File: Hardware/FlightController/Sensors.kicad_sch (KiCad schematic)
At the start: 7 parts, among them U2 MPU-6050, U5 MMC5603NJ

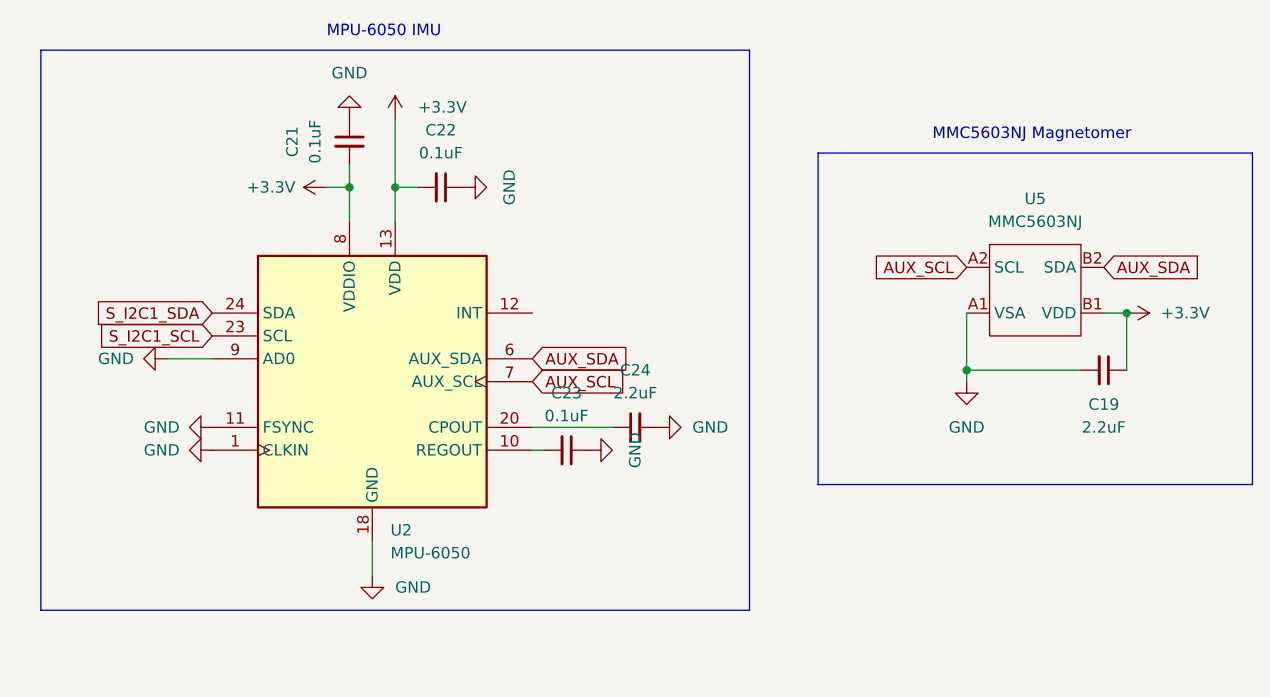
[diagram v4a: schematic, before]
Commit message: Update footprints to be digikey compliant
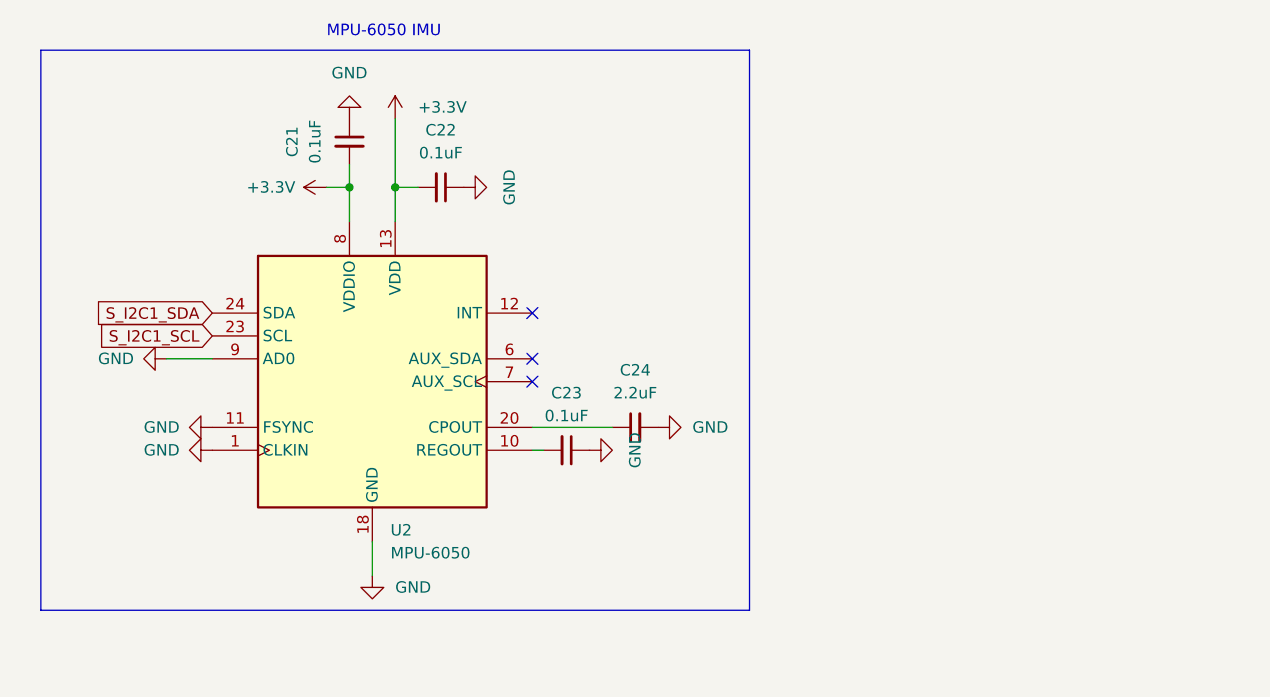
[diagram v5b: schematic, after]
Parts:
- removed C19: 2.2uF, Capacitor_SMD:C_0402_1005Metric, symbol Device:C_Small
- removed U5: MMC5603NJ, Package_BGA:WLP-4_0.83x0.83mm_P0.4mm, symbol FlightControllerLibrary:MMC5603NJ
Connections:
- net AUX_SCL: no longer names the net of U2.7 (AUX_SCL)
- net AUX_SDA: no longer names the net of U2.6 (AUX_SDA)
- no-connect marks 0 -> 3
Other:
- note removed: "MMC5603NJ Magnetomer"
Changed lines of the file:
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@@
   (junction (at 58.42 33.02) (diameter 0) (color 0 0 0 0)
   )
-  (junction (at 121.92 53.34) (diameter 0) (color 0 0 0 0)
-  )
   (junction (at 53.34 33.02) (diameter 0) (color 0 0 0 0)
   )
-  (junction (at 139.7 46.99) (diameter 0) (color 0 0 0 0)
-  )
+  (no_connect (at 73.66 54.61))
+  (no_connect (at 73.66 52.07))
+  (no_connect (at 73.66 46.99))
   (polyline (pts (xy 19.05 80.01) (xy 19.05 17.78))
     (stroke (width 0) (type default) (color 0 0 0 0))
@@
     (stroke (width 0) (type default) (color 0 0 0 0))
   )
-  (wire (pts (xy 121.92 53.34) (xy 134.62 53.34))
-    (stroke (width 0) (type default) (color 0 0 0 0))
-  )
-  (polyline (pts (xy 153.67 66.04) (xy 105.41 66.04))
-    (stroke (width 0) (type default) (color 0 0 0 0))
-  )
-  (polyline (pts (xy 105.41 66.04) (xy 105.41 29.21))
-    (stroke (width 0) (type default) (color 0 0 0 0))
-  )
   (wire (pts (xy 53.34 33.02) (xy 53.34 36.83))
     (stroke (width 0) (type default) (color 0 0 0 0))
   )
-  (wire (pts (xy 137.16 46.99) (xy 139.7 46.99))
-    (stroke (width 0) (type default) (color 0 0 0 0))
-  )
   (wire (pts (xy 55.88 76.2) (xy 55.88 72.39))
     (stroke (width 0) (type default) (color 0 0 0 0))
@@
     (stroke (width 0) (type default) (color 0 0 0 0))
   )
-  (wire (pts (xy 121.92 53.34) (xy 121.92 54.61))
-    (stroke (width 0) (type default) (color 0 0 0 0))
-  )
   (polyline (pts (xy 97.79 80.01) (xy 19.05 80.01))
     (stroke (width 0) (type default) (color 0 0 0 0))
   )
-  (polyline (pts (xy 153.67 29.21) (xy 153.67 66.04))
-    (stroke (width 0) (type default) (color 0 0 0 0))
-  )
-  (wire (pts (xy 139.7 46.99) (xy 139.7 53.34))
-    (stroke (width 0) (type default) (color 0 0 0 0))
-  )
   (wire (pts (xy 58.42 33.02) (xy 58.42 36.83))
     (stroke (width 0) (type default) (color 0 0 0 0))
   )
-  (wire (pts (xy 121.92 46.99) (xy 121.92 53.34))
-    (stroke (width 0) (type default) (color 0 0 0 0))
-  )
   (polyline (pts (xy 97.79 17.78) (xy 97.79 80.01))
     (stroke (width 0) (type default) (color 0 0 0 0))
@@
     (stroke (width 0) (type default) (color 0 0 0 0))
   )
-  (polyline (pts (xy 105.41 29.21) (xy 153.67 29.21))
-    (stroke (width 0) (type default) (color 0 0 0 0))
-  )
   (text "MPU-6050 IMU" (at 50.8 16.51 0)
-    (effects (font (size 1.27 1.27)) (justify left bottom))
-  )
-  (text "MMC5603NJ Magnetomer" (at 118.11 27.94 0)
     (effects (font (size 1.27 1.27)) (justify left bottom))
   )
@@
     )
   )
-  (global_label "AUX_SCL" (shape input) (at 73.66 54.61 0) (fields_autoplaced)
-    (effects (font (size 1.27 1.27)) (justify left))
-    (property "Intersheet References" "${INTERSHEET_REFS}" (id 0) (at 84.1769 54.6894 0)
-      (effects (font (size 1.27 1.27)) (justify left) hide)
-    )
-  )
-  (global_label "AUX_SDA" (shape input) (at 137.16 41.91 0) (fields_autoplaced)
-    (effects (font (size 1.27 1.27)) (justify left))
-    (property "Intersheet References" "${INTERSHEET_REFS}" (id 0) (at 147.7374 41.8306 0)
-      (effects (font (size 1.27 1.27)) (justify left) hide)
-    )
-  )
-  (global_label "AUX_SCL" (shape input) (at 121.92 41.91 180) (fields_autoplaced)
-    (effects (font (size 1.27 1.27)) (justify right))
-    (property "Intersheet References" "${INTERSHEET_REFS}" (id 0) (at 111.4031 41.8306 0)
-      (effects (font (size 1.27 1.27)) (justify right) hide)
-    )
-  )
-  (global_label "AUX_SDA" (shape input) (at 73.66 52.07 0) (fields_autoplaced)
-    (effects (font (size 1.27 1.27)) (justify left))
-    (property "Intersheet References" "${INTERSHEET_REFS}" (id 0) (at 84.2374 51.9906 0)
-      (effects (font (size 1.27 1.27)) (justify left) hide)
-    )
-  )
   (symbol (lib_id "power:+3.3V") (at 58.42 25.4 0) (unit 1)
     (in_bom yes) (on_board yes) (fields_autoplaced)
@@
     )
     (property "Datasheet" "" (id 3) (at 58.42 25.4 0)
-      (effects (font (size 1.27 1.27)) hide)
-    )
-    (pin "1")
-  )
-  (symbol (lib_id "power:+3.3V") (at 139.7 46.99 270) (unit 1)
-    (in_bom yes) (on_board yes) (fields_autoplaced)
-    (property "Reference" "#PWR023" (id 0) (at 135.89 46.99 0)
-      (effects (font (size 1.27 1.27)) hide)
-    )
-    (property "Value" "+3.3V" (id 1) (at 143.51 46.9899 90)
-      (effects (font (size 1.27 1.27)) (justify left))
-    )
-    (property "Footprint" "" (id 2) (at 139.7 46.99 0)
-      (effects (font (size 1.27 1.27)) hide)
-    )
-    (property "Datasheet" "" (id 3) (at 139.7 46.99 0)
       (effects (font (size 1.27 1.27)) hide)
     )
@@
     (pin "2")
   )
-  (symbol (lib_id "Device:C_Small") (at 137.16 53.34 270) (unit 1)
-    (in_bom yes) (on_board yes)
-    (property "Reference" "C19" (id 0) (at 137.16 57.15 90))
-    (property "Value" "2.2uF" (id 1) (at 137.16 59.69 90))
-    (property "Footprint" "Capacitor_SMD:C_0402_1005Metric" (id 2) (at 137.16 53.34 0)
-      (effects (font (size 1.27 1.27)) hide)
-    )
-    (property "Datasheet" "~" (id 3) (at 137.16 53.34 0)
-      (effects (font (size 1.27 1.27)) hide)
-    )
-    (pin "1")
-    (pin "2")
-  )
   (symbol (lib_id "Device:C_Small") (at 63.5 33.02 270) (unit 1)
     (in_bom yes) (on_board yes) (fields_autoplaced)
@@
     (pin "2")
   )
-  (symbol (lib_id "FlightControllerLibrary:MMC5603NJ") (at 129.54 44.45 0) (unit 1)
-    (in_bom yes) (on_board yes) (fields_autoplaced)
-    (property "Reference" "U5" (id 0) (at 129.54 34.29 0))
-    (property "Value" "MMC5603NJ" (id 1) (at 129.54 36.83 0))
-    (property "Footprint" "Package_BGA:WLP-4_0.83x0.83mm_P0.4mm" (id 2) (at 129.54 44.45 0)
-      (effects (font (size 1.27 1.27)) hide)
-    )
-    (property "Datasheet" "" (id 3) (at 129.54 44.45 0)
-      (effects (font (size 1.27 1.27)) hide)
-    )
-    (pin "A1")
-    (pin "A2")
-    (pin "B1")
-    (pin "B2")
-  )
   (symbol (lib_id "Device:C_Small") (at 53.34 27.94 0) (unit 1)
     (in_bom yes) (on_board yes) (fields_autoplaced)
@@
       (effects (font (size 1.27 1.27)) hide)
     )
-    (pin "1")
-  )
-  (symbol (lib_id "power:GND") (at 121.92 54.61 0) (unit 1)
-    (in_bom yes) (on_board yes) (fields_autoplaced)
-    (property "Reference" "#PWR022" (id 0) (at 121.92 60.96 0)
-      (effects (font (size 1.27 1.27)) hide)
-    )
-    (property "Value" "GND" (id 1) (at 121.92 59.69 0))
-    (property "Footprint" "" (id 2) (at 121.92 54.61 0)
-      (effects (font (size 1.27 1.27)) hide)
-    )
-    (property "Datasheet" "" (id 3) (at 121.92 54.61 0)
-      (effects (font (size 1.27 1.27)) hide)
-    )

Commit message: Update footprints, routing and LCSC numbers
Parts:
- C11: renamed from C21; footprint Capacitor_SMD:C_0402_1005Metric -> Capacitor_SMD:C_0603_1608Metric_Pad1.08x0.95mm_HandSolder; dk (none) -> y
- C12: renamed from C22; footprint Capacitor_SMD:C_0402_1005Metric -> Capacitor_SMD:C_0603_1608Metric_Pad1.08x0.95mm_HandSolder; dk (none) -> y
- C13: renamed from C23; footprint Capacitor_SMD:C_0402_1005Metric -> Capacitor_SMD:C_0603_1608Metric_Pad1.08x0.95mm_HandSolder; dk (none) -> y
- C14: renamed from C24; LCSC (none) -> C12530
- U4: renamed from U2; LCSC (none) -> C24112
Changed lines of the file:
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@@
   (symbol (lib_id "power:+3.3V") (at 58.42 25.4 0) (unit 1)
     (in_bom yes) (on_board yes) (fields_autoplaced)
-    (property "Reference" "#PWR034" (id 0) (at 58.42 29.21 0)
+    (property "Reference" "#PWR024" (id 0) (at 58.42 29.21 0)
       (effects (font (size 1.27 1.27)) hide)
     )
@@
   (symbol (lib_id "power:GND") (at 33.02 52.07 270) (unit 1)
     (in_bom yes) (on_board yes)
-    (property "Reference" "#PWR028" (id 0) (at 26.67 52.07 0)
+    (property "Reference" "#PWR018" (id 0) (at 26.67 52.07 0)
       (effects (font (size 1.27 1.27)) hide)
     )
@@
   (symbol (lib_id "power:GND") (at 66.04 33.02 90) (unit 1)
     (in_bom yes) (on_board yes) (fields_autoplaced)
-    (property "Reference" "#PWR035" (id 0) (at 72.39 33.02 0)
+    (property "Reference" "#PWR025" (id 0) (at 72.39 33.02 0)
       (effects (font (size 1.27 1.27)) hide)
     )
@@
   (symbol (lib_id "Device:C_Small") (at 85.09 59.69 90) (unit 1)
     (in_bom yes) (on_board yes) (fields_autoplaced)
-    (property "Reference" "C24" (id 0) (at 85.0963 53.34 90))
+    (property "Reference" "C14" (id 0) (at 85.0963 53.34 90))
     (property "Value" "2.2uF" (id 1) (at 85.0963 55.88 90))
     (property "Footprint" "Capacitor_SMD:C_0402_1005Metric" (id 2) (at 85.09 59.69 0)
@@
       (effects (font (size 1.27 1.27)) hide)
     )
+    (property "LCSC" "C12530" (id 4) (at 85.09 59.69 0)
+      (effects (font (size 1.27 1.27)) hide)
+    )
     (pin "1")
     (pin "2")
@@
   (symbol (lib_id "power:+3.3V") (at 50.8 33.02 90) (unit 1)
     (in_bom yes) (on_board yes)
-    (property "Reference" "#PWR031" (id 0) (at 54.61 33.02 0)
+    (property "Reference" "#PWR021" (id 0) (at 54.61 33.02 0)
       (effects (font (size 1.27 1.27)) hide)
     )
@@
   (symbol (lib_id "Sensor_Motion:MPU-6050") (at 55.88 54.61 0) (unit 1)
     (in_bom yes) (on_board yes) (fields_autoplaced)
-    (property "Reference" "U2" (id 0) (at 57.8994 71.12 0)
+    (property "Reference" "U4" (id 0) (at 57.8994 71.12 0)
       (effects (font (size 1.27 1.27)) (justify left))
     )
@@
     )
     (property "Datasheet" "https://store.invensense.com/datasheets/invensense/MPU-6050_DataSheet_V3%204.pdf" (id 3) (at 55.88 58.42 0)
+      (effects (font (size 1.27 1.27)) hide)
+    )
+    (property "LCSC" "C24112" (id 4) (at 55.88 54.61 0)
       (effects (font (size 1.27 1.27)) hide)
     )
@@
   (symbol (lib_id "power:GND") (at 87.63 59.69 90) (unit 1)
     (in_bom yes) (on_board yes) (fields_autoplaced)
-    (property "Reference" "#PWR037" (id 0) (at 93.98 59.69 0)
+    (property "Reference" "#PWR027" (id 0) (at 93.98 59.69 0)
       (effects (font (size 1.27 1.27)) hide)
     )
@@
   (symbol (lib_id "Device:C_Small") (at 77.47 62.23 270) (unit 1)
     (in_bom yes) (on_board yes) (fields_autoplaced)
-    (property "Reference" "C23" (id 0) (at 77.4636 55.88 90))
+    (property "Reference" "C13" (id 0) (at 77.4636 55.88 90))
     (property "Value" "0.1uF" (id 1) (at 77.4636 58.42 90))
-    (property "Footprint" "Capacitor_SMD:C_0402_1005Metric" (id 2) (at 77.47 62.23 0)
+    (property "Footprint" "Capacitor_SMD:C_0603_1608Metric_Pad1.08x0.95mm_HandSolder" (id 2) (at 77.47 62.23 0)
       (effects (font (size 1.27 1.27)) hide)
     )
@@
       (effects (font (size 1.27 1.27)) hide)
     )
+    (property "dk" "y" (id 4) (at 77.47 62.23 0)
+      (effects (font (size 1.27 1.27)) hide)
+    )
     (pin "1")
     (pin "2")
@@
   (symbol (lib_id "Device:C_Small") (at 63.5 33.02 270) (unit 1)
     (in_bom yes) (on_board yes) (fields_autoplaced)
-    (property "Reference" "C22" (id 0) (at 63.4936 26.67 90))
+    (property "Reference" "C12" (id 0) (at 63.4936 26.67 90))
     (property "Value" "0.1uF" (id 1) (at 63.4936 29.21 90))
-    (property "Footprint" "Capacitor_SMD:C_0402_1005Metric" (id 2) (at 63.5 33.02 0)
+    (property "Footprint" "Capacitor_SMD:C_0603_1608Metric_Pad1.08x0.95mm_HandSolder" (id 2) (at 63.5 33.02 0)
       (effects (font (size 1.27 1.27)) hide)
     )
@@
       (effects (font (size 1.27 1.27)) hide)
     )
+    (property "dk" "y" (id 4) (at 63.5 33.02 0)
+      (effects (font (size 1.27 1.27)) hide)
+    )
     (pin "1")
     (pin "2")
@@
   (symbol (lib_id "Device:C_Small") (at 53.34 27.94 0) (unit 1)
     (in_bom yes) (on_board yes) (fields_autoplaced)
-    (property "Reference" "C21" (id 0) (at 46.99 27.9464 90))
+    (property "Reference" "C11" (id 0) (at 46.99 27.9464 90))
     (property "Value" "0.1uF" (id 1) (at 49.53 27.9464 90))
-    (property "Footprint" "Capacitor_SMD:C_0402_1005Metric" (id 2) (at 53.34 27.94 0)
+    (property "Footprint" "Capacitor_SMD:C_0603_1608Metric_Pad1.08x0.95mm_HandSolder" (id 2) (at 53.34 27.94 0)
       (effects (font (size 1.27 1.27)) hide)
     )
@@
       (effects (font (size 1.27 1.27)) hide)
     )
+    (property "dk" "y" (id 4) (at 53.34 27.94 0)
+      (effects (font (size 1.27 1.27)) hide)
+    )
     (pin "1")
     (pin "2")
@@
   (symbol (lib_id "power:GND") (at 38.1 62.23 270) (unit 1)
     (in_bom yes) (on_board yes)
-    (property "Reference" "#PWR030" (id 0) (at 31.75 62.23 0)
+    (property "Reference" "#PWR020" (id 0) (at 31.75 62.23 0)
       (effects (font (size 1.27 1.27)) hide)
     )
@@
   (symbol (lib_id "power:GND") (at 55.88 76.2 0) (unit 1)
     (in_bom yes) (on_board yes) (fields_autoplaced)
-    (property "Reference" "#PWR033" (id 0) (at 55.88 82.55 0)
+    (property "Reference" "#PWR023" (id 0) (at 55.88 82.55 0)
       (effects (font (size 1.27 1.27)) hide)
     )
@@
   (symbol (lib_id "power:GND") (at 38.1 59.69 270) (unit 1)
     (in_bom yes) (on_board yes)
-    (property "Reference" "#PWR029" (id 0) (at 31.75 59.69 0)
+    (property "Reference" "#PWR019" (id 0) (at 31.75 59.69 0)
       (effects (font (size 1.27 1.27)) hide)
     )
@@
   (symbol (lib_id "power:GND") (at 80.01 62.23 90) (unit 1)
     (in_bom yes) (on_board yes) (fields_autoplaced)
-    (property "Reference" "#PWR036" (id 0) (at 86.36 62.23 0)
+    (property "Reference" "#PWR026" (id 0) (at 86.36 62.23 0)
       (effects (font (size 1.27 1.27)) hide)
     )
@@
   (symbol (lib_id "power:GND") (at 53.34 25.4 180) (unit 1)
     (in_bom yes) (on_board yes) (fields_autoplaced)
-    (property "Reference" "#PWR032" (id 0) (at 53.34 19.05 0)
-      (effects (font (size 1.27 1.27)) hide)
-    )
+    (property "Reference" "#PWR022" (id 0) (at 53.34 19.05 0)
+      (effects (font (size 1.27 1.27)) hide)
+    )
